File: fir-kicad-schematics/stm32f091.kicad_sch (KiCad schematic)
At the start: 3 parts, among them U2 STM32F091RCTx

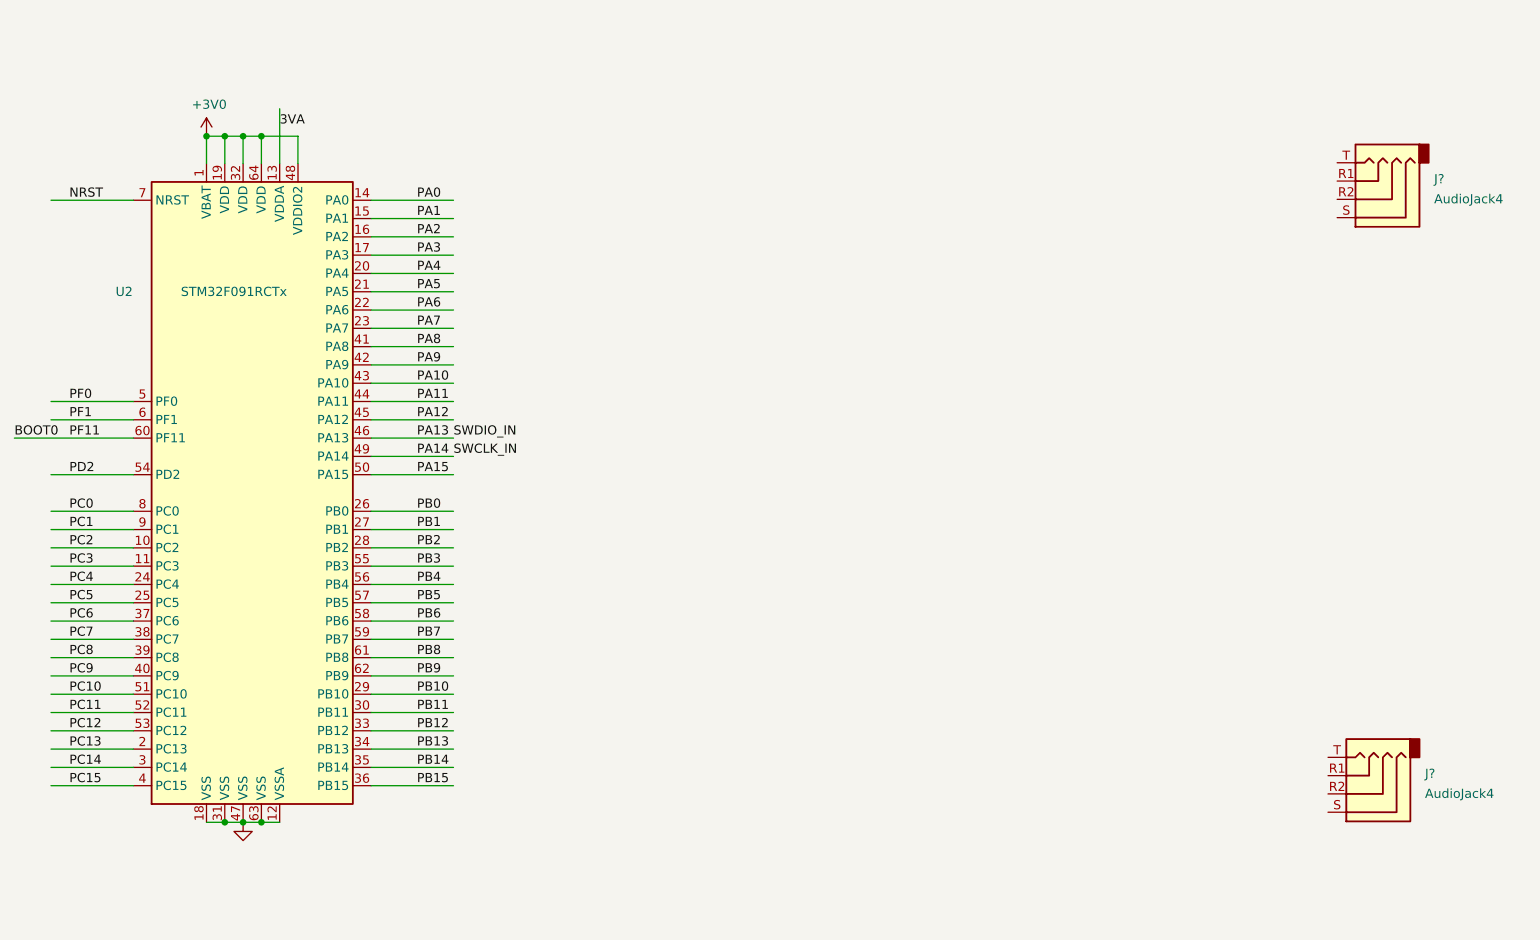
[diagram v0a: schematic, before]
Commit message: Finished schematic and generated PDF
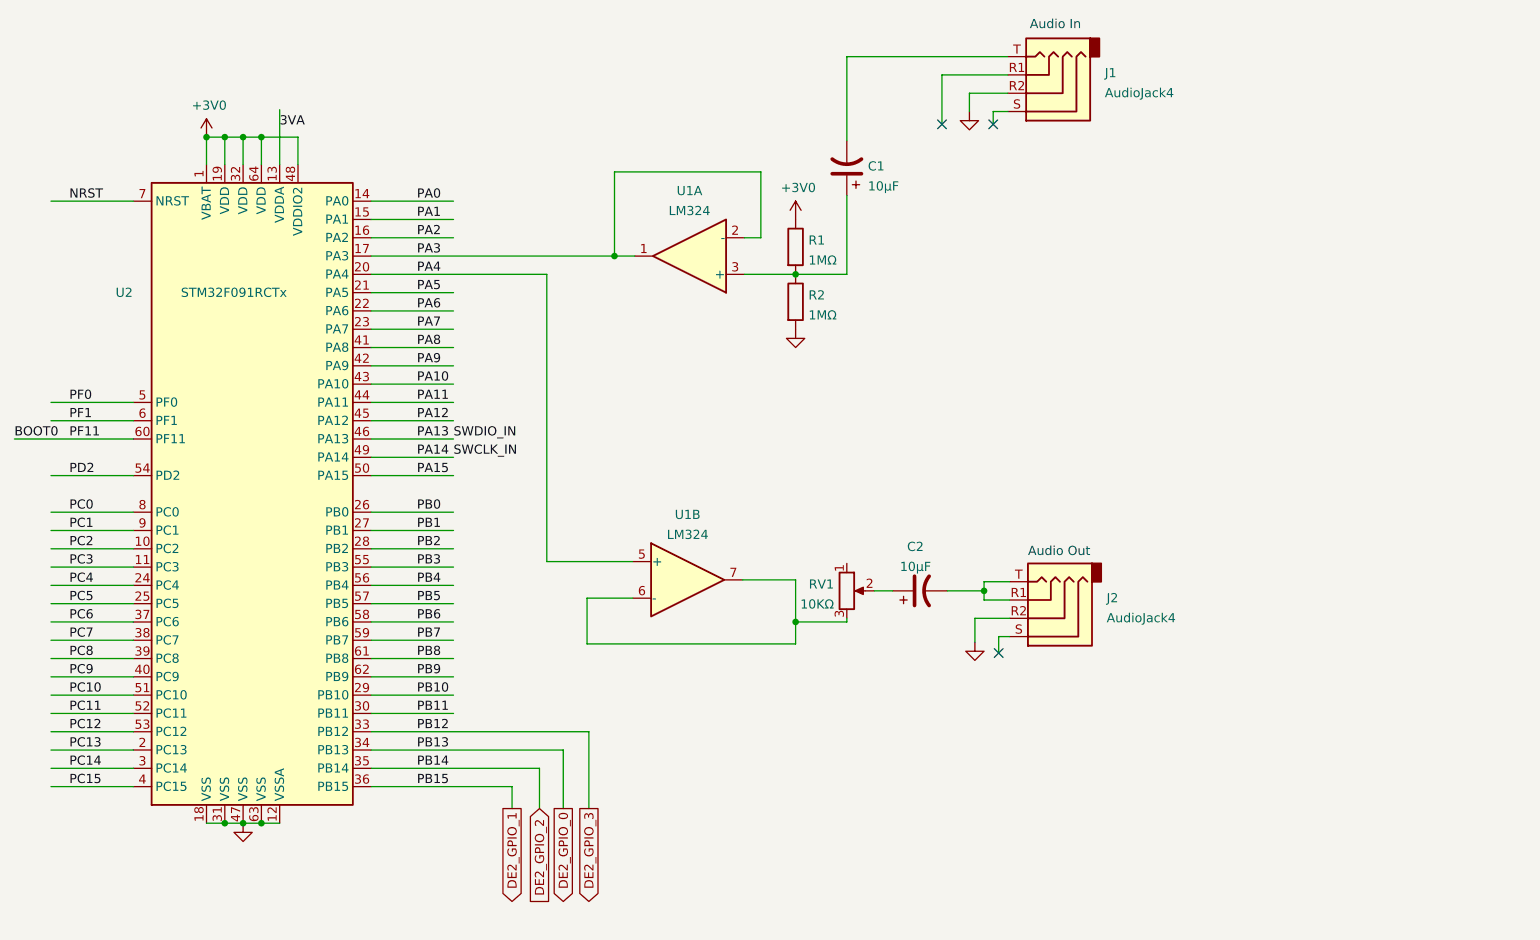
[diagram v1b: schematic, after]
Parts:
- removed J?: AudioJack4, symbol Connector:AudioJack4
- added C1, C2: 10µF, symbol Device:C_Polarized_US
- added J2: AudioJack4, symbol Connector:AudioJack4
- added R1, R2: 1MΩ, symbol Device:R
- added RV1: 10KΩ, symbol Device:R_Potentiometer
- added U1: LM324, symbol Amplifier_Operational:LM324
- gave numbers to parts that had none: 1
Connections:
- net +3V0: now also R1.1
- net GND: now also J1.R2, J2.R2, R2.2
- net PA3: now also U1.1, U1.2 (-)
- net PA4: now also U1.5 (+)
- net at J1.T: now also C1.2
- net PB12 renamed DE2_GPIO_3
- net PB13 renamed DE2_GPIO_0
- net PB14 renamed DE2_GPIO_2
- net PB15 renamed DE2_GPIO_1
- new net: RV1.3, U1.6 (-), U1.7
- new net: C2.1, RV1.2
- new net: C1.1, R1.2, R2.1, U1.3 (+)
- new net: C2.2, J2.R1, J2.T
- no-connect marks 0 -> 3
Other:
- note added: "Audio In"
- note added: "Audio Out"
- moved on the sheet: J1
